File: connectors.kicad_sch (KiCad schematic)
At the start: 10 parts, among them J1 Conn_01x10, J10 USB B connector, J12 RJ45, J2 Conn_01x10, J3 Conn_01x10, J4 Conn_01x10, J7 Conn_01x10, J8 Conn_01x10, J9 RJ45

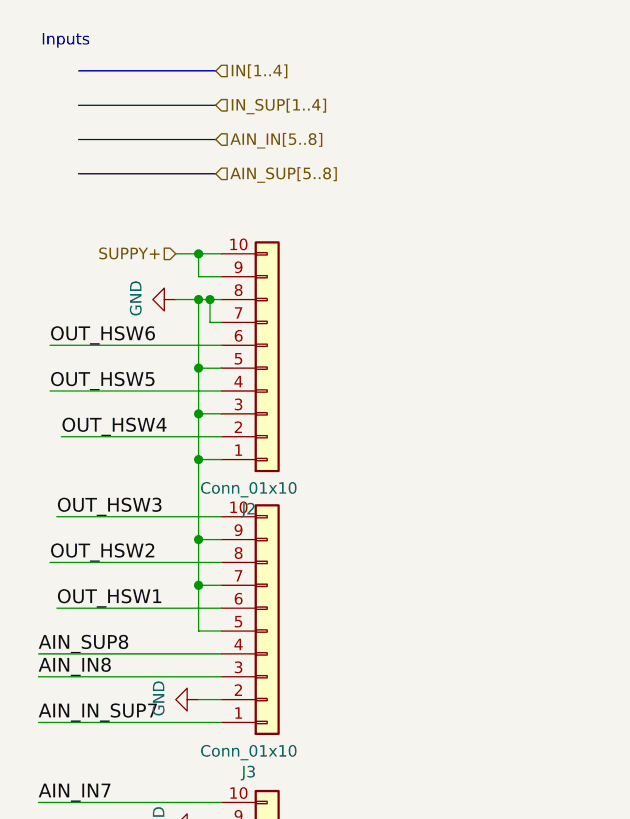
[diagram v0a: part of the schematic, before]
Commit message: UPDATE - LAN chipset waiting for verification
Signed-off-by: Jacek <matuszewski.kartech@gmail.com>
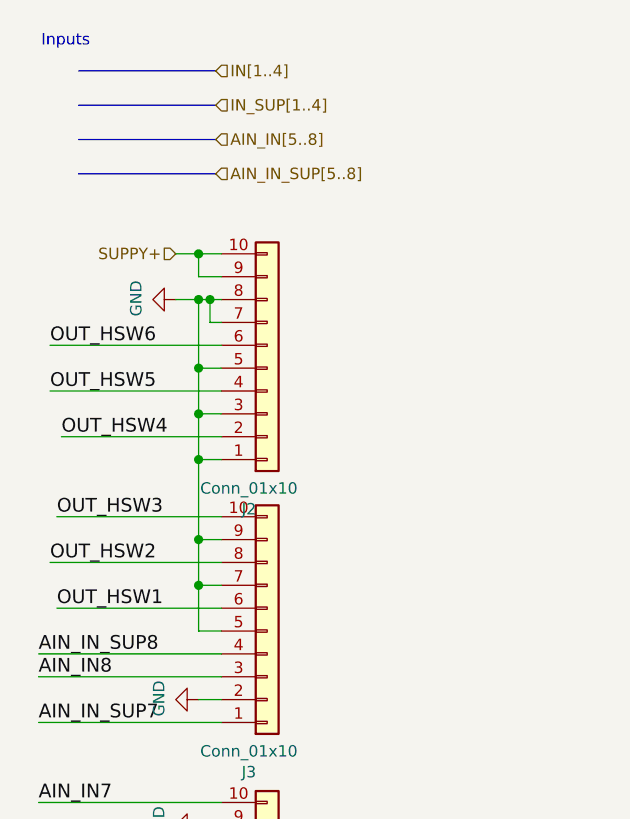
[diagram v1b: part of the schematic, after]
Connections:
- net AIN_SUP8 renamed AIN_IN_SUP8
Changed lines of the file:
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@@
 (kicad_sch (version 20201015) (generator eeschema)
-  (page 1 12)
   (paper "A4")
   (junction (at 41.275 68.58) (diameter 1.016) (color 0 0 0 0))
@@
     (effects (font (size 1.27 1.27)) (justify right bottom))
   )
-  (label "AIN_SUP8" (at 23.495 113.03 0)
+  (label "AIN_IN_SUP8" (at 23.495 113.03 0)
     (effects (font (size 1.524 1.524)) (justify left bottom))
   )
@@
     (effects (font (size 1.27 1.27)) (justify left))
   )
-  (hierarchical_label "AIN_SUP[5..8]" (shape input) (at 43.18 59.69 0)
+  (hierarchical_label "AIN_IN_SUP[5..8]" (shape input) (at 43.18 59.69 0)
     (effects (font (size 1.27 1.27)) (justify left))
   )

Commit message: Fixes
Signed-off-by: Jarosław Karwik <jaroslaw.karwik@gmail.com>
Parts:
- J12, J9: TME (none) -> 54602-910LF
- R49: TME WF06P-120R-5% -> (none)
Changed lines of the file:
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@@
       (effects (font (size 1.27 1.27)) hide)
     )
-    (property "TME" "WF06P-120R-5% " (id 4) (at 203.2 93.98 90)
+    (property "TME" "" (id 4) (at 203.2 93.98 90)
       (effects (font (size 1.27 1.27)) hide)
     )
@@
       (effects (font (size 1.27 1.27)) hide)
     )
+    (property "TME" "54602-910LF" (id 4) (at 200.66 45.72 0)
+      (effects (font (size 1.27 1.27)) hide)
+    )
   )
   (symbol (lib_id "Connector:RJ45") (at 224.79 45.72 270) (unit 1)
@@
       (effects (font (size 1.27 1.27)) hide)
     )
+    (property "TME" "54602-910LF" (id 4) (at 224.79 45.72 0)
+      (effects (font (size 1.27 1.27)) hide)
+    )

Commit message: UPDATE - 3D and Jumper descriptions
Signed-off-by: Jacek <matuszewski.kartech@gmail.com>
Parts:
- added J15, J16, J17, J18, J19, J20: Conn_01x10, symbol Uni_Printer-rescue:Conn_01x10-Connector_Generic
- J1, J2, J3, J4, J7, J8: TME (none) -> 15EDGRC-3.5/10P; TME-GNIAZDO 15EDGRC-3.5/10P -> (none); TME-WTYK 15EDGK-3.5/10P -> (none)
- R49: TME (none) -> SMD0603-0R
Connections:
- no-connect marks 0 -> 60
